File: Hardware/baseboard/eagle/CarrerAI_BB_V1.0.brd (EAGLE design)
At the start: 59 x 58 mm, 201 parts, among them X1 JST-4POS-2X4POS, X1.2 TACH/LAP, X2.2 VRAILS+, X2.3 SoC, X4 SYSTEMI-SW, X5 87758-0816, X6 87758-0616, X7 SYSTEMI-SE, X8 STMI-CW/GPIO

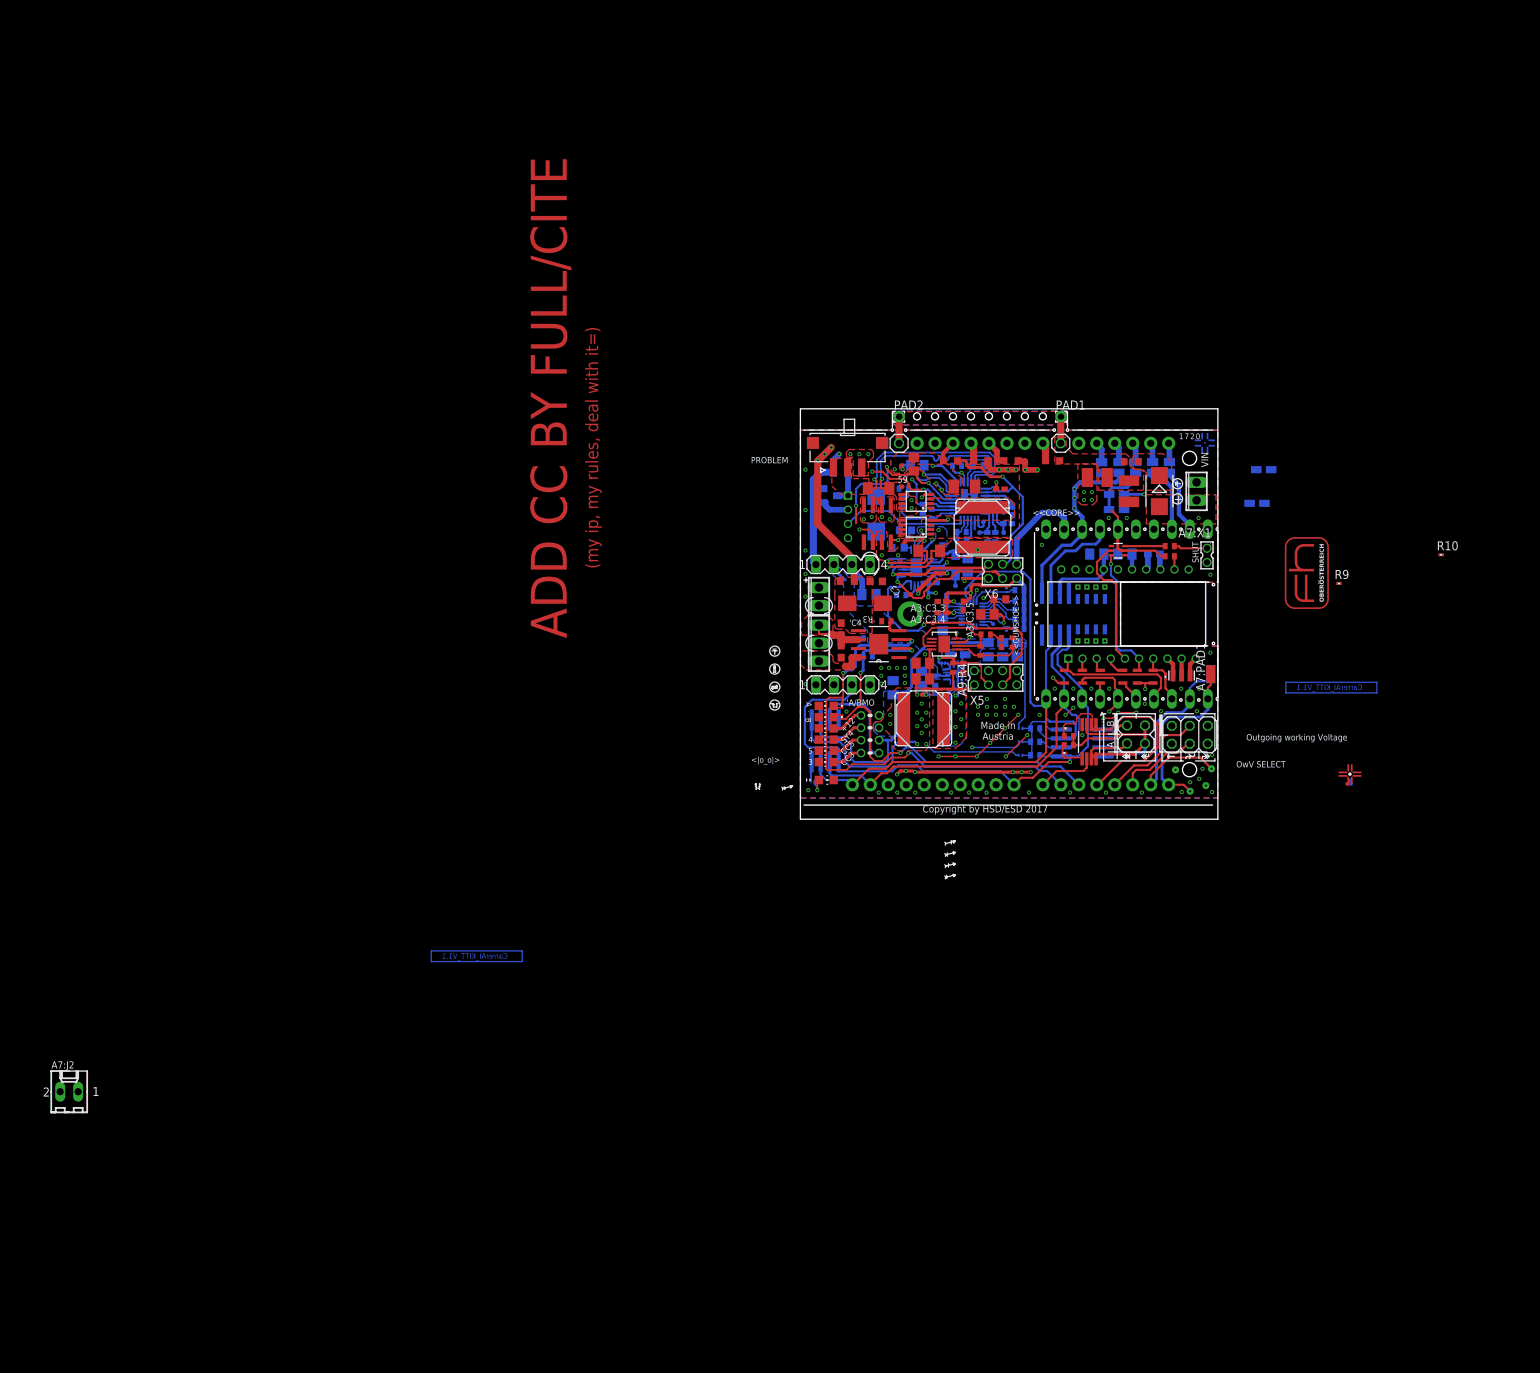
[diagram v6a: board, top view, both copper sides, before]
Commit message: Baseboard SV3.01
Changelog:
 +> added usb again because I was bored
 +> adjusted some routes in the center
 +> I2C VBUS selector has been improved
 +> after reexamination of the cad model, there is a slack on the north
    and south side by a a few millimeters, which makes things easier.
    That's what one gets for assuming things.

Message of the Day:
 _____________________________________
/ You are not dead yet. But watch for \
\ further reports.                    /
 -------------------------------------
  \
   \
       __
      UooU\.'@@@@@@`.
      \__/(@@@@@@@@@@)
           (@@@@@@@@)
           `YY~~~~YY'
            ||    ||
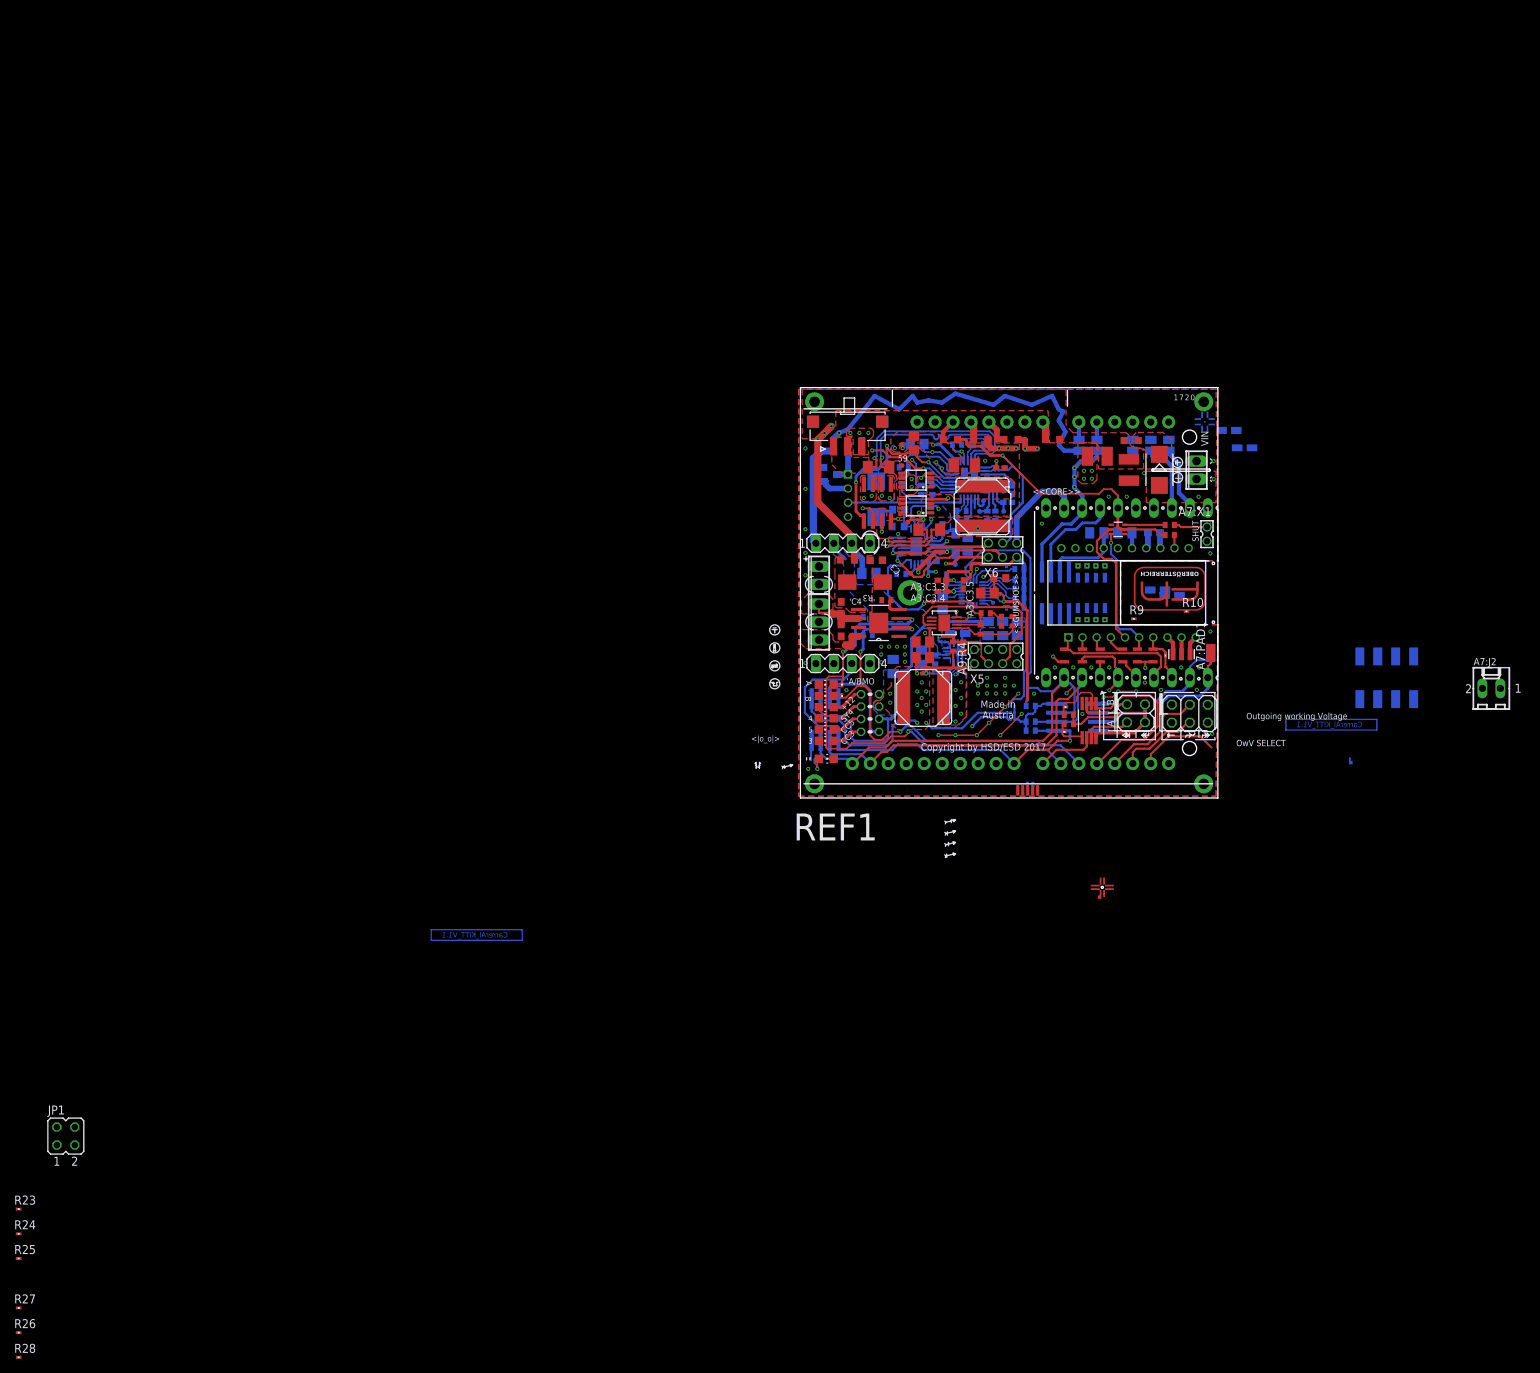
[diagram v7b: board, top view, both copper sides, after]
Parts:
- removed JP2: (no value), pinhead:1X01
- removed PAD1, PAD2: (no value), wirepad:1,6/0,9
- added R21, R22, R23, R24, R25, R26, R27, R28: (no value), rcl:R0201
- added REF1: REF.EDULIMIT, kitt.refs:REF_EAGLE.EDULIMIT
- added SWX.1, SWX.2, SWX.3, SWX.4, SWX.5, SWX.6, SWX.7, SWX.8: (no value), wirepad:SMD1,27-2,54
- added U$2: 1051330011, kitt.con:POS-5
- JP1: device pinhead:1X01 -> jumper:JP2Q
- moved A7:J2 208.9 mm to (97.7, 15.5)
- moved JP1 171.4 mm to (-103.8, -47.8)
- moved R10 36.9 mm to (54.6, 26.4)
- moved R9 29.4 mm to (47.1, 25.3)
- moved A4:R2 22.7 mm to (50.5, 29.4)
- moved A4:R3 20.1 mm to (62.8, 49.5)
- moved A10:REF2 19.5 mm to (52.2, 29.6), turned to 180 degrees
- moved A4:R4 18.3 mm to (60.6, 51.9)
- moved A4:R1 17.7 mm to (52.5, 28.6)
- moved R20 6.12 mm to (30.0, 12.0)
- moved A7:⌁20 5.90 mm to (34.7, 17.0)
- moved ☈1 4.50 mm to (39.4, 49.8)
- moved ☈2 4.40 mm to (41.9, 49.8)
- moved A7:⌁18 3.93 mm to (39.8, 17.0)
- moved A7:⌁19 3.93 mm to (37.3, 17.0)
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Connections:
- removed net UNO.ADC1: XA1.ADC.1, ☈1.2
- removed net UNO.ADC2: XA1.ADC.2, ☈2.2
- new net N$18: XA1.ADC.1, ☈2.2
- new net N$19: XA1.ADC.0, ☈1.2
- new net N$20: R22.1, U$2.3
- new net N$21: R21.1, U$2.2
- new net N$22: R23.1, R27.1, U$2.1
- new net N$23: R27.2, U$2.4
- new net N$24: R22.2, R24.2
- new net N$25: R21.2, R25.2
- net +18V: no longer JP1.1, JP2.1, PAD1.1, PAD2.1
- net GND: now also U$2.5
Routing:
- net +4.1V: track 41.3 -> 88.7 mm
- net +3V3: track 144.9 -> 124.4 mm, vias 16 -> 10
- net TOP.!RST: track 37.9 -> 55.8 mm
- net +18V: track 70.1 -> 52.7 mm
- net TOP.OS1IS2: track 9.63 -> 26.1 mm
- net TOP.RRX: track 25.0 -> 12.5 mm, vias 1 -> 0
- net TOP.MTXS: track 32.8 -> 23.7 mm, vias 1 -> 0
- net SYSTWI.SDA: track 93.0 -> 84.0 mm
- net TOP.MVPRW: track 8.64 -> 0.00 mm
- net SYSTWI.SCL: track 121.5 -> 115.3 mm
- net SYSTWI.!INT: track 92.1 -> 87.2 mm
- net VSYS: track 91.4 -> 87.0 mm
- net UNO.ADC1: track 2.92 -> 0.00 mm
- net UNO.ADC2: track 2.88 -> 0.00 mm
- net UNO.ADC3: track 2.82 -> 0.00 mm
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- removed copper zone on layer 15, net +18V
- removed copper zone on layer 16, net +18V
- removed copper zone on layer 2, net +18V
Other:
- outline, holes or cut-outs redrawn
- board text added: "60V"
- board text added: "park gap!"
- board text removed: "(my ip, my rules, deal with it=)"
- board text removed: "ADD CC BY FULL/CITE"
- board text removed: "PROBLEM"
- board text removed: "XTRA FUL SYSTEWI"
- board text removed: "for tracer"
- board text removed: "hold it! make breakaway , really ridicuously long jumper PCB!"
- board text removed: "mount on bottom"

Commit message: Baseboard v3.XYZ ---- 1. Whoever called the ambulance, thanks I guess?    Thank your lucky stars I don't have to pay up.    2.6 %/100 nothing serious. 2. Work is never over, also I am bored at the AKH Linz what else am I to do?
Message of the Morning:
 __________________________________
/ Be cheerful while you are alive. \
|                                  |
\ -- Phathotep, 24th Century B.C.  /
 ----------------------------------
 \              /\
  \             )~)
    /\/\       ( (
   ( oo )_-------_)
    \__/         )
     \/ /|/---\|\
      .. ..  ..  ..
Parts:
- removed A5:☇9, A6:☇6, A6:☇7, A6:☇8, A6:☇9: PTR1TP07R, testpad:TP07R
- removed R23, R24, R25, R26, R27, R28: (no value), rcl:R0201
- removed SWX.1, SWX.2, SWX.3, SWX.4, SWX.5, SWX.6, SWX.7, SWX.8: (no value), wirepad:SMD1,27-2,54
- removed U$2: 1051330011, kitt.con:POS-5
- removed ☈1, ☈10, ☈11, ☈2, ☈3: (no value), jumper:SJ
- added A4:A1:OK2: Si8710, optocoupler:DIL06
- added A4:A1:R13, A4:A1:R14: (no value), rcl:MINI_MELF-0207R
- added A4:A1:R16: (no value), rcl:R0402
- added A4:B3: DBDB102G, rectifier:DB
- added A4:R5: VARISTORCN1206, varistor:CT/CN1206
- added A4:R6: VARISTORCN1210, varistor:CT/CN1210
- added A7:LED1, A7:LED2: (no value), led:LZR181
- added A7:MEC1: MEC.HAL4711/OPTICS, kitt.refs:MEC.HAL4711
- added A7:R10, A7:R11: 200R, rcl:R0402
- added JMP1, JMP2: 0R-JUMPA, jump-0r-smd:A0R-JMP
- added L3, L6: CM CHOKE, rcl:L3216C
- added S2, S6: 219-04, switch-dil:CTS-219-04
- added S4: (no value), switch:255SB
- added S5: 9450-2, switch-misc:9450-2
- added X3:R1, X3:R2, X3:R21, X3:R22, X3:R23, X3:R24, X3:R25, X3:R26, X3:R27, X3:R28, X3:R29, X3:R3, X3:R4, X3:R5: (no value), rcl:R0201
- added X3:U$2: 1051330011, kitt.con:POS-5
- added X9: 87758-0616, con-molex:87758-0616
- moved JP1 277.2 mm to (142.2, 79.9)
- moved R22 131.0 mm to (148.6, 61.8), flipped to the top, turned to 0 degrees
- moved R21 129.8 mm to (147.0, 63.7), flipped to the top, turned to 0 degrees
- moved R9 86.8 mm to (133.8, 21.3)
- moved R10 79.6 mm to (134.2, 26.8)
- moved A7:J2 75.1 mm to (142.7, 75.5)
- moved A4:R4 23.5 mm to (37.3, 48.6), turned to 270 degrees
- moved A4:R1 22.5 mm to (42.0, 48.5), turned to 90 degrees
- moved A4:R2 22.0 mm to (39.5, 48.5), turned to 270 degrees
- moved A4:R3 19.3 mm to (43.5, 48.5), turned to 90 degrees
- moved A10:REF2 13.4 mm to (38.8, 29.0), turned to 0 degrees
- moved A7:PAD1 10.8 mm to (68.8, 20.8)
- moved A7:PAD2 9.85 mm to (67.8, 20.8)
- moved A7:DCL2 6.75 mm to (35.2, 22.4)
- moved A4:C1 5.49 mm to (41.0, 46.7), turned to 90 degrees
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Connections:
- net A7:N$8 renamed A7:SHUT
- removed net N$20: R22.1, U$2.3
- removed net N$21: R21.1, U$2.2
- removed net N$22: R23.1, R27.1, U$2.1
- removed net N$23: R27.2, U$2.4
- removed net N$24: R22.2, R24.2
- removed net N$25: R21.2, R25.2
- new net A4:A1:GND: A4:A1:OK2.4, A4:A1:R14.1
- new net A4:A1:MRXS: A4:A1:OK2.1
- new net A4:A1:N$1: A4:A1:OK2.5, A4:A1:R13.1, A4:A1:R16.2
- new net A4:A1:N$2: A4:A1:OK2.2, A4:A1:R14.2
- new net A4:A1:N$3: A4:A1:OK2.6, A4:A1:R16.1
- new net A4:A1:V+++: A4:A1:R13.2
- new net A7:N$2: A7:LED1.K, A7:R10.2
- new net A7:OD\!SHUT: A7:R10.1, A7:R11.1, A7:R7.1, A7:U2.6
- new net AUX.USB/D+_P: JMP2.1, X3:R24.1
- new net AUX.USB/D-_N: JMP1.1, X3:R25.1
- new net N$17: A4:B3.AC1, L6.2
- new net N$5: L3.1, L6.1, X2.2.2
- new net UNO.RX: JMP1.2, XA1.IO.0
- new net UNO.TX: JMP2.2, XA1.IO.1
- new net X3:B-ID: X3:R27.2, X3:R5.1, X3:U$2.4
- new net X3:N$5: X3:R22.2, X3:R24.2
- new net X3:N$6: X3:R21.2, X3:R25.2, X3:R26.2, X3:R28.2
- new net X3:O>D+: X3:R22.1, X3:U$2.3
- new net X3:O>D-: X3:R21.1, X3:U$2.2
- new net X3:O>VBUS: X3:R23.1, X3:R27.1, X3:R29.1, X3:U$2.1
- net +18V: now also A4:B3.+, A4:R5.2
- net +3V3: now also A7:LED1.A, A7:LED2.A
- net +4.1V: no longer ☈1.1
- net +5V: now also X3:R23.2
- net A7:N$1: now also A7:LED2.K, A7:R11.2; no longer A7:R7.1, A7:U2.6
- net CORE.ADCX: no longer ☈10.1
- net CORE.ADCY: no longer ☈11.1
- net DDC.CLN/VIN: no longer A5:☇9.TP
- net GND: now also A4:R5.1, L3.2, X3:R1.1, X3:R1.2, X3:R2.1, X3:R2.2, X3:R26.1, X3:R28.1, X3:R3.1, X3:R3.2, X3:R4.1, X3:R4.2, X3:R5.2, X3:U$2.5; no longer U$2.5, X2.2.2
- net N$18: no longer ☈2.2
- net N$19: no longer ☈1.2
- net TOP.FREQ: no longer A6:☇6.TP
- net TOP.MODE: no longer A6:☇9.TP
- net TOP.MTXS: now also JMP2.3; no longer XA1.IO.1
- net TOP.MVPRW: no longer ☈3.1
- net TOP.PGOOD: no longer A6:☇7.TP
- net TOP.RRX: now also JMP1.3; no longer XA1.IO.0
- net TOP.RUN: no longer A6:☇8.TP
- net UNO.ADC3: no longer ☈3.2
- net UNO.ADC4: no longer ☈10.2
- net UNO.ADC5: no longer ☈11.2
- net VCC/2: now also A4:B3.AC2
- net VSYS: now also X3:R29.2; no longer ☈2.1
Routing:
- net +4.1V: track 88.7 -> 12.8 mm
- net VSYS: track 87.0 -> 140.1 mm, vias 23 -> 26
- net SYSTWI.!INT: track 87.2 -> 123.0 mm, vias 2 -> 4
- net SYSTWI.SDA: track 84.0 -> 119.6 mm, vias 1 -> 2
- net A7:OD\!SHUT: track 0.00 -> 33.6 mm, vias 0 -> 2
- net ITH: track 21.2 -> 36.5 mm
- net AUX.USB/D-_N: track 0.00 -> 15.2 mm
- net X3:O>VBUS: track 0.00 -> 14.9 mm
- net A7:N$2: track 0.00 -> 14.3 mm
- net +3V3: track 124.4 -> 113.3 mm, vias 10 -> 13
- net CORE.ADCX: track 10.8 -> 0.00 mm
- net TOP.MTXS: track 23.7 -> 13.9 mm
- net AUX.USB/D+_P: track 0.00 -> 9.61 mm
- net CORE.ADCY: track 9.60 -> 0.00 mm
- net TOP.RRX: track 12.5 -> 22.0 mm
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- added copper zone on layer 15, net +18V
- added copper zone on layer 15, net +5V
- removed copper zone on layer 1, net +18V
- removed copper zone on layer 15, net +24V
- removed copper zone on layer 15, net VF+OUT/IPC
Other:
- outline, holes or cut-outs redrawn
- board text added: "<<GUMSTK>>"
- board text added: "HAL4711"
- board text added: "I CANT LET YOU DO THAT, ESDAVE."
- board text removed: "<<GUMSHOE>>"
